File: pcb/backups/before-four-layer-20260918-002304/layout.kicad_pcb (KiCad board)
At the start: 4 copper layers, 36 x 76 mm, 115 parts, among them J1 B2B-PH-K-S, J3 B2B-PH-K-S, J4 104031-0811, Q1 AO3400A, Q2 AO3400A, SW1 PTS841GKSMTR LFS, SW2 JS202011AQN, U1 113991114, U10 SN74CBTLV3245APWR, U11 SN74CBTLV3245APWR, U3 MAX17048G+T10, U4 BMI270, U5 TPS61023DRLR, U6 AP2112K-3.3TRG1, U7 TPS22918DBVR, U8 TPS22918DBVR, U9 TPS22918DBVR

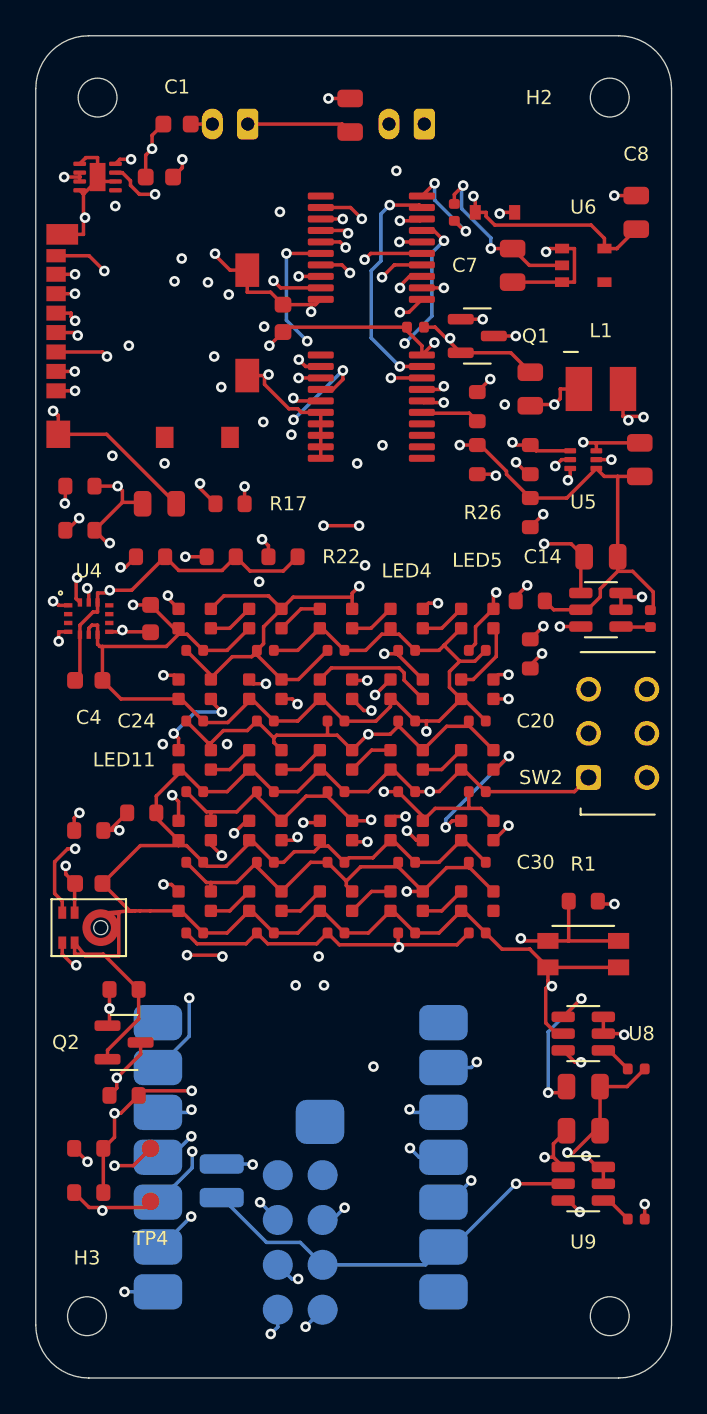
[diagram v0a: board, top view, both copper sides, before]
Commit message: Update board configuration, BOM, and documentation for new XIAO ESP32S3
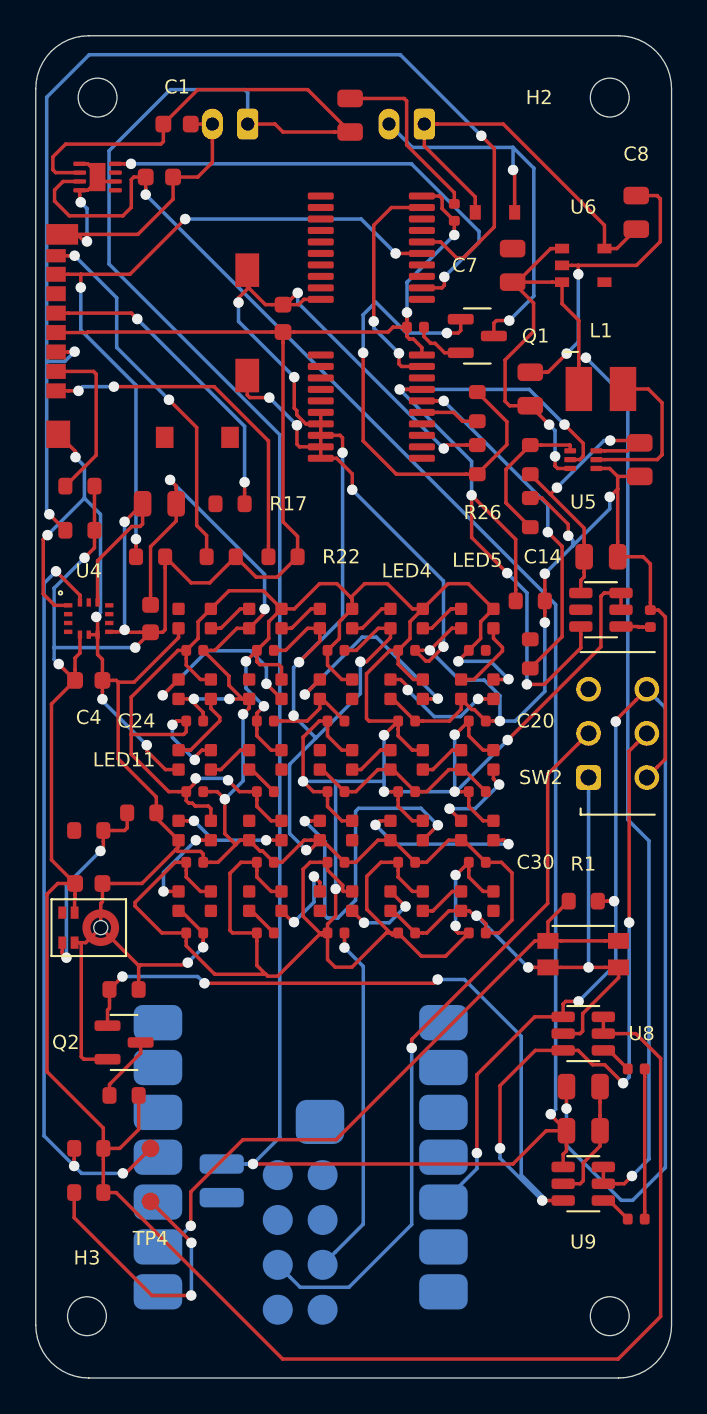
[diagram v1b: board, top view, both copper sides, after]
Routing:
- net VBAT: track 110.1 -> 197.5 mm, vias 4 -> 3
- net FG_SCL: track 86.8 -> 16.2 mm, vias 5 -> 2
- net HOST_PDM_DATA: track 67.8 -> 0.00 mm, vias 4 -> 0
- net HOST_PDM_CLK: track 63.5 -> 0.00 mm, vias 7 -> 0
- net HOST_IMU_INT: track 60.2 -> 0.00 mm, vias 2 -> 0
- net HOST_SD_CS: track 59.8 -> 0.00 mm, vias 2 -> 0
- net HOST_HAPTIC: track 59.5 -> 0.00 mm, vias 4 -> 0
- net HOST_SD_MOSI: track 58.1 -> 0.00 mm, vias 2 -> 0
- net ISOLATE_N: track 73.0 -> 16.7 mm, vias 4 -> 2
- net HOST_SD_CLK: track 55.0 -> 0.00 mm, vias 2 -> 0
- net HOST_SD_MISO: track 54.8 -> 0.00 mm, vias 2 -> 0
- net LED_5V: track 175.9 -> 229.1 mm, vias 12 -> 17
- net HOST_SDA: track 53.1 -> 0.00 mm, vias 2 -> 0
- net HOST_SCL: track 52.9 -> 0.00 mm, vias 3 -> 0
- net HOST_LED_ENABLE: track 51.9 -> 0.00 mm, vias 2 -> 0
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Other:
- copper layers 4 -> 2
